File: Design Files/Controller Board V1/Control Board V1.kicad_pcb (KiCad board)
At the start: 2 copper layers, 1 part, among them U1 MIC29752WWT

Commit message: Added to Control Board Schematic
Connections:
- U1 pad 1: unconnected-(U1-EN-Pad1) -> +24V
- U1 pad 2: unconnected-(U1-IN-Pad2) -> +24V
- U1 pad 3: unconnected-(U1-GND-Pad3) -> P,GND
- U1 pad 4: unconnected-(U1-OUT-Pad4) -> +15V
- U1 pad 5: unconnected-(U1-ADJ-Pad5) -> Net-(U1-ADJ)
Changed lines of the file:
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@@
 	)
 	(net 0 "")
-	(net 1 "unconnected-(U1-OUT-Pad4)")
-	(net 2 "unconnected-(U1-ADJ-Pad5)")
-	(net 3 "unconnected-(U1-EN-Pad1)")
-	(net 4 "unconnected-(U1-IN-Pad2)")
-	(net 5 "unconnected-(U1-GND-Pad3)")
+	(net 1 "+15V")
+	(net 2 "Net-(U1-ADJ)")
+	(net 3 "+24V")
+	(net 4 "P,GND")
 	(footprint "MIC29752WWT:TO-247-5_MCH"
 		(layer "F.Cu")
@@
 			(layers "*.Cu" "*.Mask")
 			(remove_unused_layers no)
-			(net 3 "unconnected-(U1-EN-Pad1)")
+			(net 3 "+24V")
 			(pinfunction "EN")
 			(pintype "input")
@@
 			(layers "*.Cu" "*.Mask")
 			(remove_unused_layers no)
-			(net 4 "unconnected-(U1-IN-Pad2)")
+			(net 3 "+24V")
 			(pinfunction "IN")
 			(pintype "power_in")
@@
 			(layers "*.Cu" "*.Mask")
 			(remove_unused_layers no)
-			(net 5 "unconnected-(U1-GND-Pad3)")
+			(net 4 "P,GND")
 			(pinfunction "GND")
 			(pintype "power_out")
@@
 			(layers "*.Cu" "*.Mask")
 			(remove_unused_layers no)
-			(net 1 "unconnected-(U1-OUT-Pad4)")
+			(net 1 "+15V")
 			(pinfunction "OUT")
 			(pintype "output")
@@
 			(layers "*.Cu" "*.Mask")
 			(remove_unused_layers no)
-			(net 2 "unconnected-(U1-ADJ-Pad5)")
+			(net 2 "Net-(U1-ADJ)")
 			(pinfunction "ADJ")
 			(pintype "input")

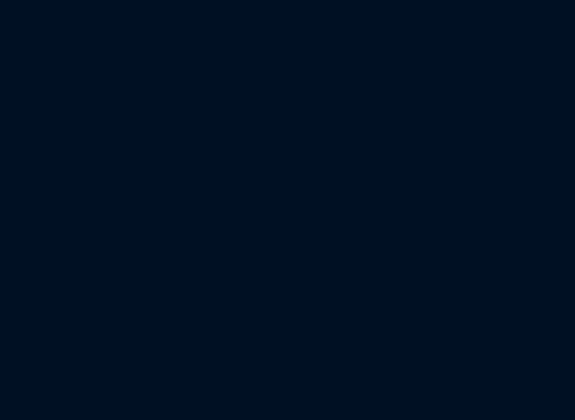
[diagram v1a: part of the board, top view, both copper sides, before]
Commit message: Added LM chip for 5V supply
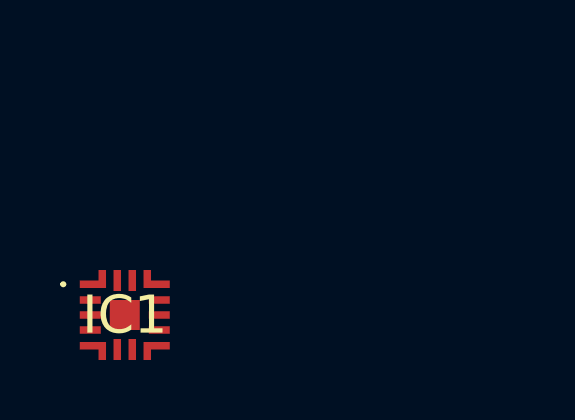
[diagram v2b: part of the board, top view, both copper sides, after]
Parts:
- added IC1: LMR66410MC5RXBRQ1, LMR66410MC5RXBRQ1:LMR66430R5RXBR, F.Cu at (95.1, 85.6)
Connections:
- U1 pad 1: +24V -> unconnected-(U1-EN-Pad1)
- U1 pad 2: +24V -> unconnected-(U1-IN-Pad2)
- U1 pad 3: P,GND -> unconnected-(U1-GND-Pad3)
- U1 pad 4: +15V -> unconnected-(U1-OUT-Pad4)
- U1 pad 5: Net-(U1-ADJ) -> unconnected-(U1-ADJ-Pad5)

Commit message: 5v supply pcb
YIPPEEEE pt2
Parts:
- added Cboot1: 100 nF, Capacitor_SMD:C_0402_1005Metric_Pad0.74x0.62mm_HandSolder, F.Cu at (166.1, 99.6)
- added Cin1: 2.2 uF, Capacitor_SMD:C_1206_3216Metric_Pad1.33x1.80mm_HandSolder, F.Cu at (172.6, 96.3)
- added Cinx1: 100 nF, Capacitor_SMD:C_0603_1608Metric_Pad1.08x0.95mm_HandSolder, F.Cu at (174.6, 96.8)
- added Cout1: 47 uF, Capacitor_SMD:C_1210_3225Metric_Pad1.33x2.70mm_HandSolder, F.Cu at (168.2, 93.1)
- added L1: 10 uH, Library:IND_TAIYO_NRS8030_TAY, F.Cu at (162.1, 94.6)
- added Rfbb1: 22.1 kOhm, Resistor_SMD:R_0402_1005Metric_Pad0.72x0.64mm_HandSolder, F.Cu at (172.2, 92.9)
- added Rfbt1: 162 kOhm, Resistor_SMD:R_0402_1005Metric_Pad0.72x0.64mm_HandSolder, F.Cu at (172.2, 91.6)
- added U1: LMR51420XDDCR, Library:SOT23_DDC_TEX, F.Cu at (168.8, 97.4)
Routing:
- net (no net): track 0.00 -> 33.3 mm, vias 0 -> 2

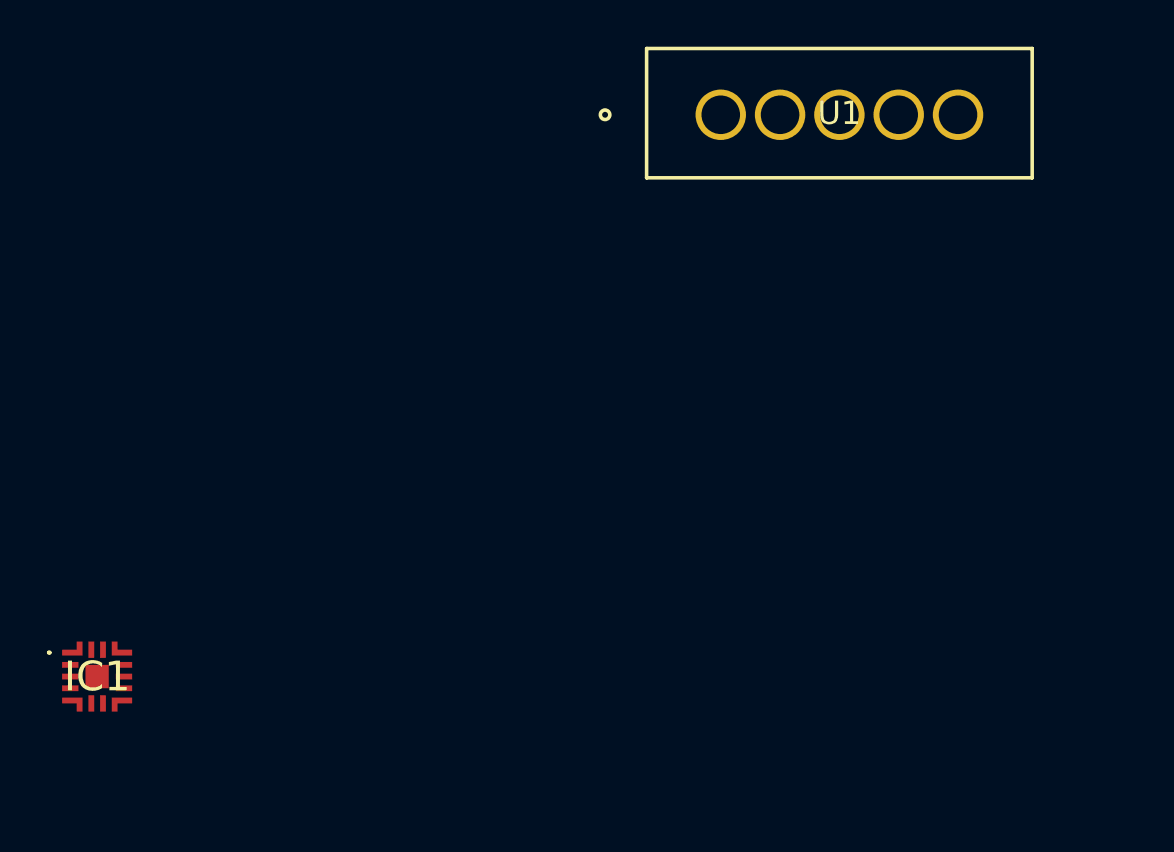
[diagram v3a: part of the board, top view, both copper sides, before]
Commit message: small tweaks to half bridge schematic
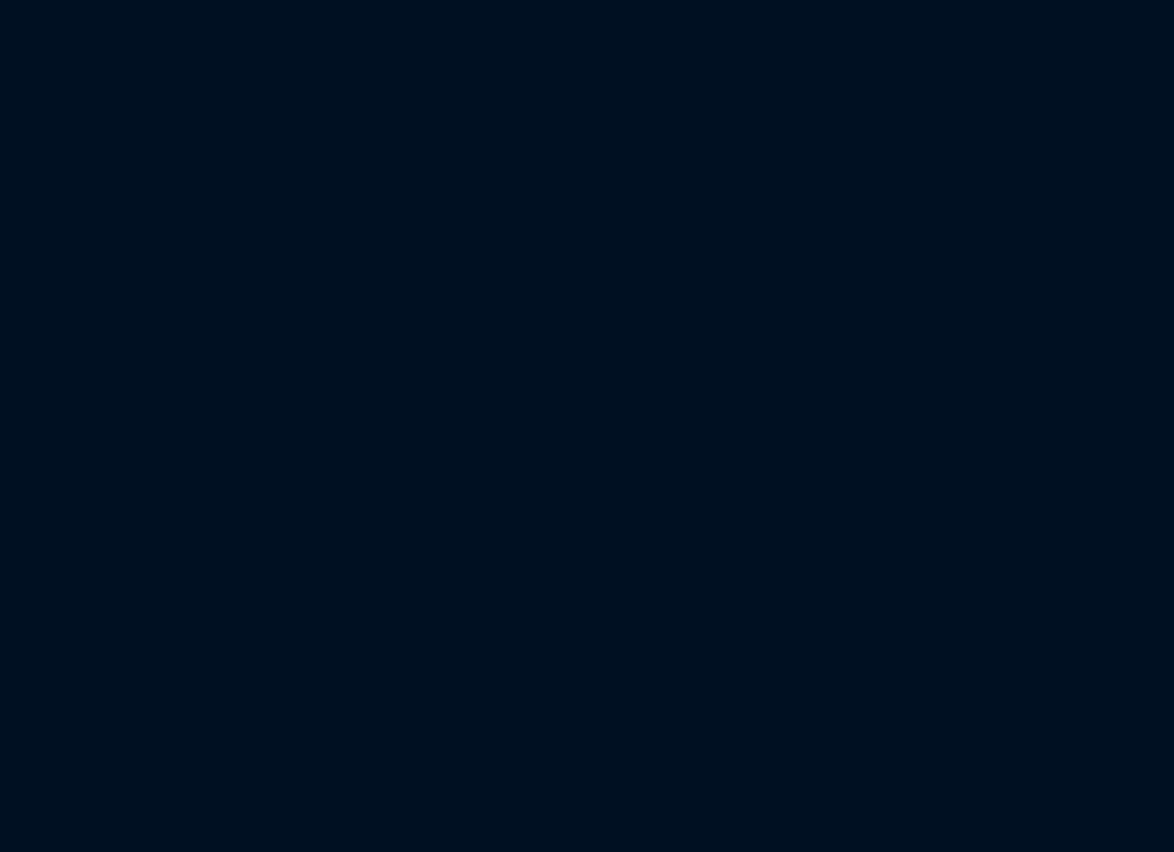
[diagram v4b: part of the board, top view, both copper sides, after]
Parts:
- removed IC1: LMR66410MC5RXBRQ1, LMR66410MC5RXBRQ1:LMR66430R5RXBR
- removed the U1 at (121.8, 61.5)

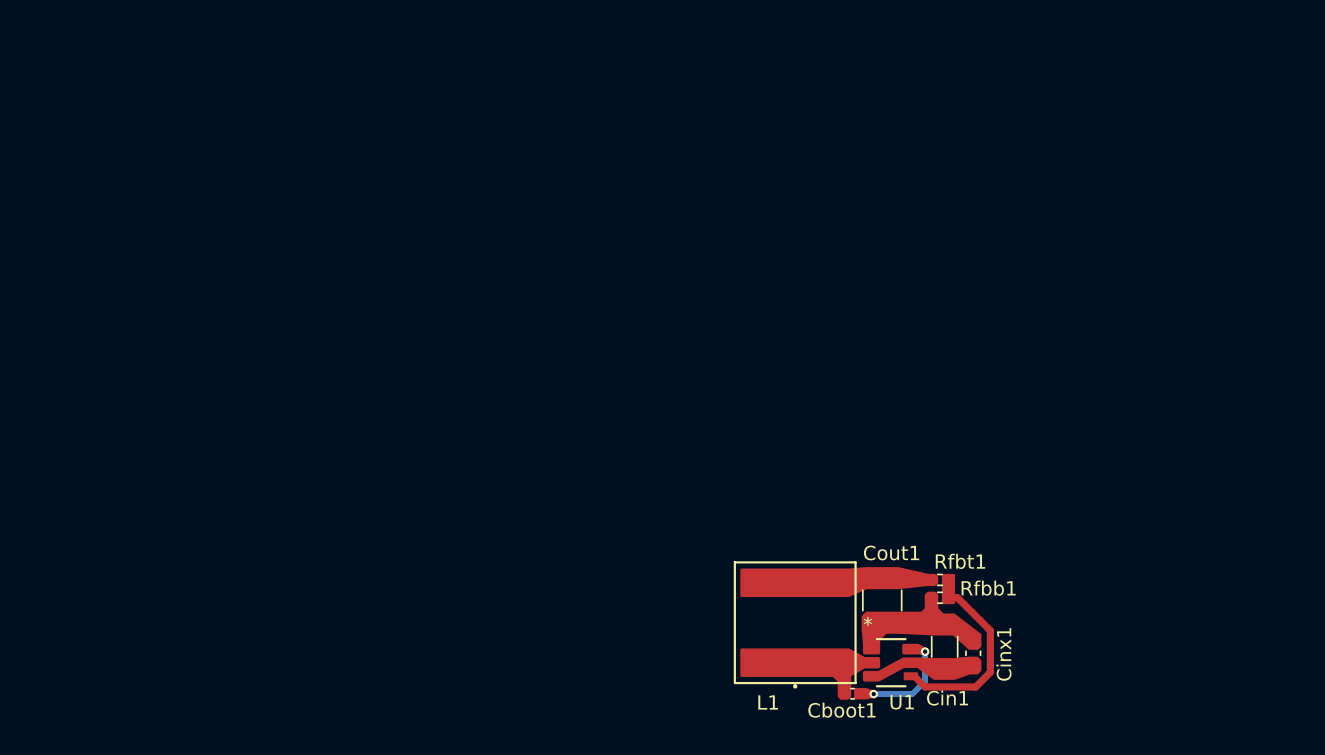
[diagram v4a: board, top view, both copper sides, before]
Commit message: Edited XT30 symbols to include solder points
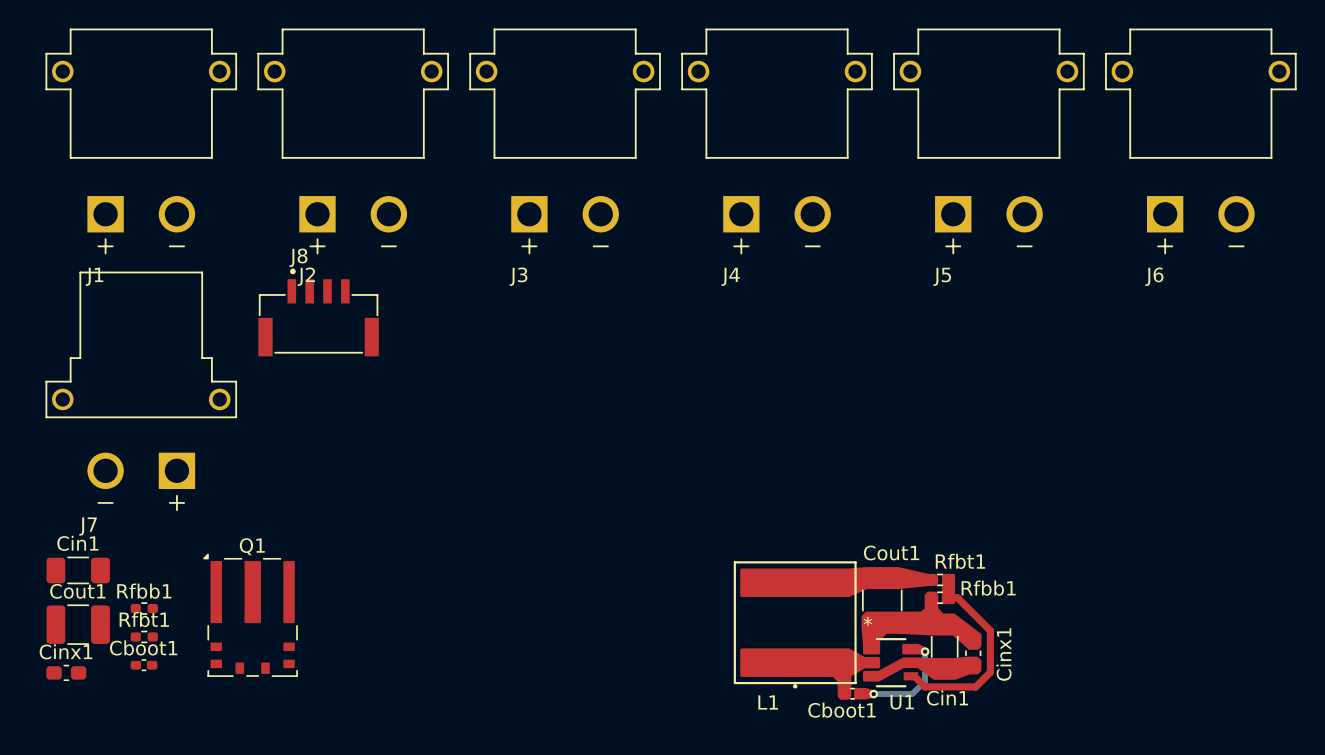
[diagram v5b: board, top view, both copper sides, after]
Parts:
- added Cboot1: 100 nF, Capacitor_SMD:C_0402_1005Metric_Pad0.74x0.62mm_HandSolder, F.Cu at (116.4, 97.6)
- added Cin1: 2.2 uF, Capacitor_SMD:C_1206_3216Metric_Pad1.33x1.80mm_HandSolder, F.Cu at (111.8, 91.0)
- added Cinx1: 100 nF, Capacitor_SMD:C_0603_1608Metric_Pad1.08x0.95mm_HandSolder, F.Cu at (111.0, 98.1)
- added Cout1: 47 uF, Capacitor_SMD:C_1210_3225Metric_Pad1.33x2.70mm_HandSolder, F.Cu at (111.8, 94.8)
- added J1: XT30PW-M, XT30PW-M:AMASS_XT30PW-M, F.Cu at (116.2, 56.0)
- added J2: XT30PW-M, XT30PW-M:AMASS_XT30PW-M, F.Cu at (131.1, 56.0)
- added J3: XT30PW-M, XT30PW-M:AMASS_XT30PW-M, F.Cu at (145.9, 56.0)
- added J4: XT30PW-M, XT30PW-M:AMASS_XT30PW-M, F.Cu at (160.8, 56.0)
- added J5: XT30PW-M, XT30PW-M:AMASS_XT30PW-M, F.Cu at (175.7, 56.0)
- added J6: XT30PW-M, XT30PW-M:AMASS_XT30PW-M, F.Cu at (190.5, 56.0)
- added J7: XT30PW-F, XT30PW-F:AMASS_XT30PW-F, F.Cu at (116.2, 79.0)
- added J8: SM04B-GHS-TB_LF__SN_-, SM04B-GHS-TB_LF__SN_-:JST_SM04B-GHS-TB_LF__SN_-, F.Cu at (128.7, 73.7)
- added Q1: LMG5200, Package_DFN_QFN:Texas_MOF0009A, F.Cu at (124.1, 94.3)
- added Rfbb1: 22.1 kOhm, Resistor_SMD:R_0402_1005Metric_Pad0.72x0.64mm_HandSolder, F.Cu at (116.5, 93.6)
- added Rfbt1: 162 kOhm, Resistor_SMD:R_0402_1005Metric_Pad0.72x0.64mm_HandSolder, F.Cu at (116.5, 95.6)

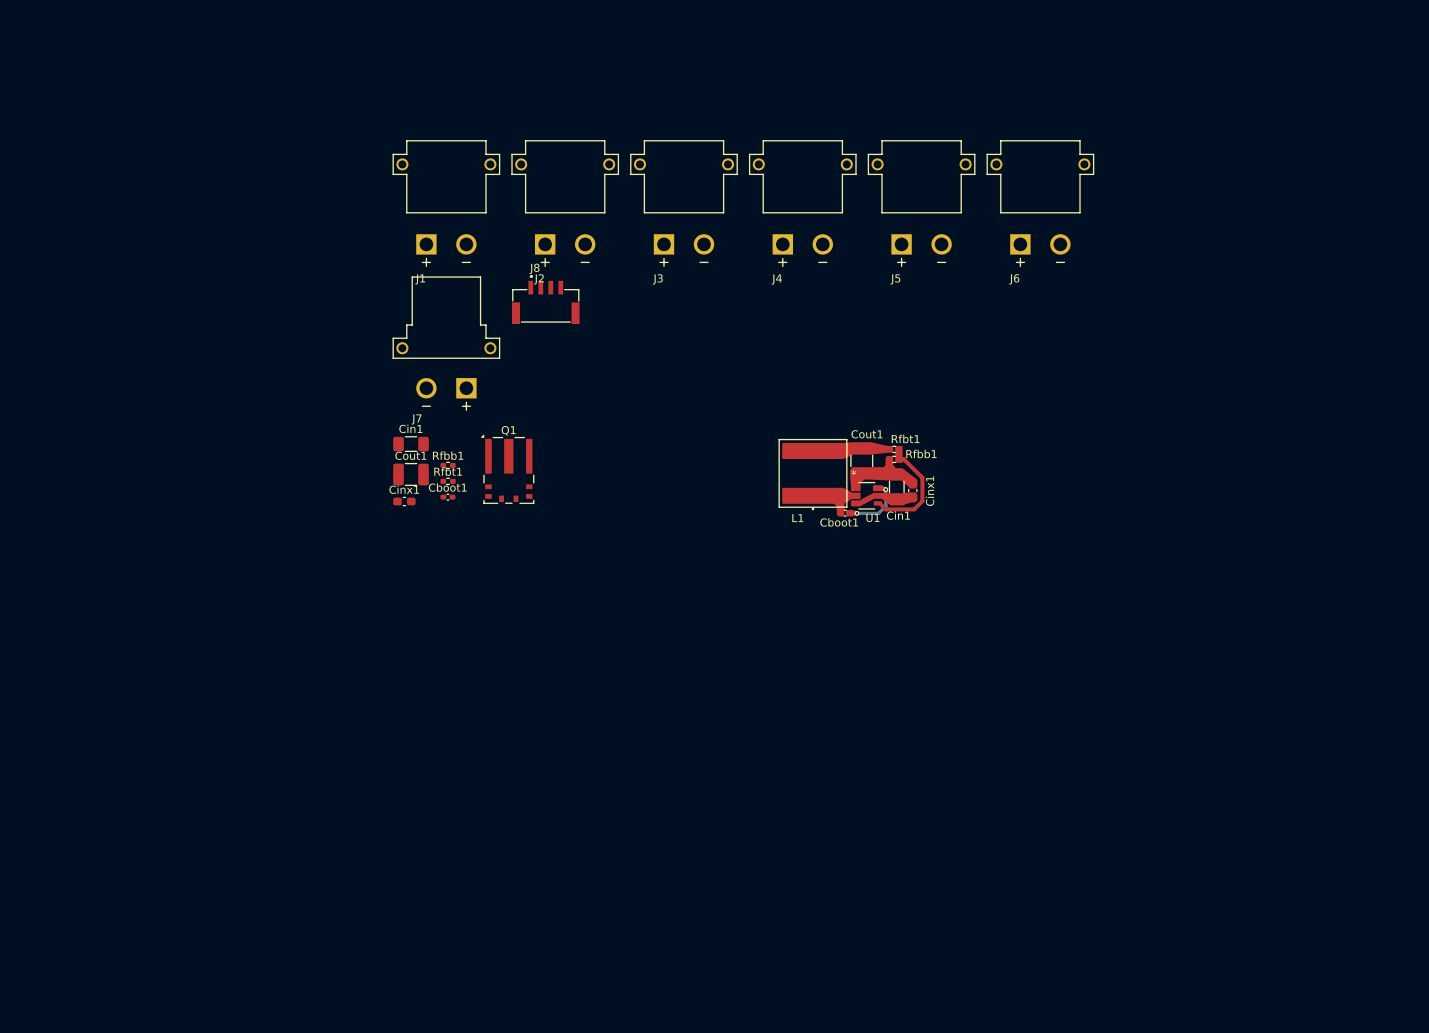
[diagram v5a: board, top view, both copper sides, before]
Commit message: Added PCB outline, mounting holes, and added design comments
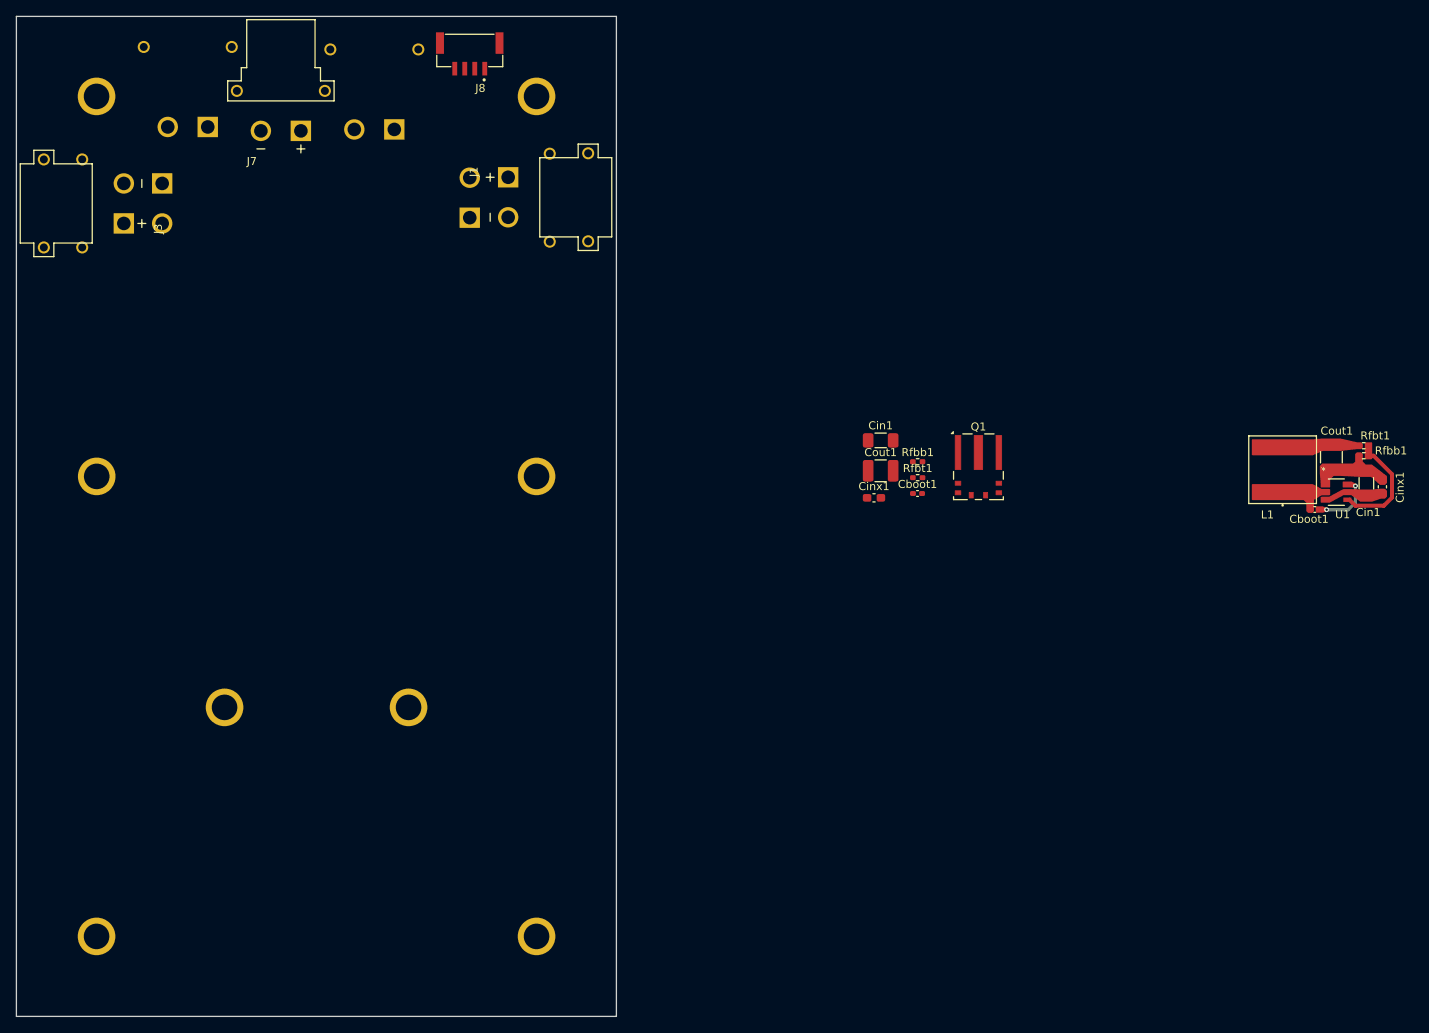
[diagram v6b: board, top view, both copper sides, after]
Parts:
- added REF**: MountingHole_3.2mm_M3, PassiveBankV1:MountingHole_3.2mm_M3, F.Cu at (88.5, 123.9)
- added REF**: MountingHole_3.2mm_M3, PassiveBankV1:MountingHole_3.2mm_M3, F.Cu at (72.5, 152.5)
- added REF**: MountingHole_3.2mm_M3, PassiveBankV1:MountingHole_3.2mm_M3, F.Cu at (111.5, 123.9)
- added REF**: MountingHole_3.2mm_M3, PassiveBankV1:MountingHole_3.2mm_M3, F.Cu at (127.5, 95.0)
- added REF**: MountingHole_3.2mm_M3, PassiveBankV1:MountingHole_3.2mm_M3, F.Cu at (127.5, 152.5)
- added REF**: MountingHole_3.2mm_M3, PassiveBankV1:MountingHole_3.2mm_M3, F.Cu at (72.5, 47.5)
- added REF**: MountingHole_3.2mm_M3, PassiveBankV1:MountingHole_3.2mm_M3, F.Cu at (127.5, 47.5)
- added REF**: MountingHole_3.2mm_M3, PassiveBankV1:MountingHole_3.2mm_M3, F.Cu at (72.5, 95.0)
- J2, J4, J5, J6: moved to B.Cu
- moved J5 92.9 mm to (83.9, 41.3), turned to 180 degrees
- moved J6 84.5 mm to (107.2, 41.6), turned to 180 degrees
- moved J3 80.2 mm to (65.9, 60.9), turned to 90 degrees
- moved J2 60.6 mm to (70.7, 60.9), turned to -90 degrees
- moved L1 58.7 mm to (220.8, 94.2)
- moved Rfbb1 58.7 mm to (230.9, 92.4)
- moved Cin1 58.7 mm to (170.5, 90.5)
- moved Cout1 58.7 mm to (170.5, 94.3)
- moved Rfbb1 58.7 mm to (175.2, 93.2)
- moved Rfbt1 58.7 mm to (175.2, 95.2)
- moved Cboot1 58.7 mm to (175.1, 97.1)
- moved Cboot1 58.7 mm to (224.8, 99.1)
- moved Cin1 58.7 mm to (231.2, 95.9)
- moved Cinx1 58.7 mm to (233.2, 96.3)
- moved Cinx1 58.7 mm to (169.7, 97.7)
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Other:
- board outline added: 75 x 125 mm
- board text added: "Cap Outline Box"
- board text added: "Put IO on this Side of Board!!!!!!!!!"

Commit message: Rough Layout started
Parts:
- added J1: XT30PW-M, XT30PW-M:AMASS_XT30PW-M, B.Cu at (109.2, 41.8)
- added J8: SM04B-GHS-TB_LF__SN_-, SM04B-GHS-TB_LF__SN_-:JST_SM04B-GHS-TB_LF__SN_-, B.Cu at (68.3, 85.4)
- added J8: SM04B-GHS-TB_LF__SN_-, SM04B-GHS-TB_LF__SN_-:JST_SM04B-GHS-TB_LF__SN_-, B.Cu at (68.3, 76.0)
- added J8: SM04B-GHS-TB_LF__SN_-, SM04B-GHS-TB_LF__SN_-:JST_SM04B-GHS-TB_LF__SN_-, B.Cu at (68.3, 66.6)
- J5: moved to F.Cu
- J8: moved to B.Cu
- moved Cin1 81.6 mm to (162.5, 139.7)
- moved Cinx1 81.6 mm to (164.5, 140.2)
- moved Cout1 81.6 mm to (158.1, 136.5)
- moved L1 81.6 mm to (152.0, 138.0)
- moved Rfbb1 81.6 mm to (162.2, 136.3)
- moved U1 81.6 mm to (158.7, 140.8)
- moved Cboot1 81.6 mm to (156.0, 143.0)
- moved Rfbt1 81.6 mm to (162.2, 135.0)
- moved J3 68.4 mm to (133.1, 73.5), turned to -90 degrees
- moved J5 67.5 mm to (133.1, 87.6), turned to -90 degrees
- moved J2 59.0 mm to (128.3, 73.5), turned to 90 degrees
- moved J8 53.2 mm to (68.3, 57.3), turned to 90 degrees
- moved J6 50.6 mm to (128.3, 87.7), turned to 90 degrees
- moved Cout1 30.3 mm to (151.1, 117.6)
- moved Rfbt1 30.3 mm to (155.7, 118.5)
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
